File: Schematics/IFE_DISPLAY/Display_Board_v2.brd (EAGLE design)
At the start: 108 x 83.8 mm, 79 parts, among them U4 HEX_CONVERTER, U5 HEX_CONVERTER

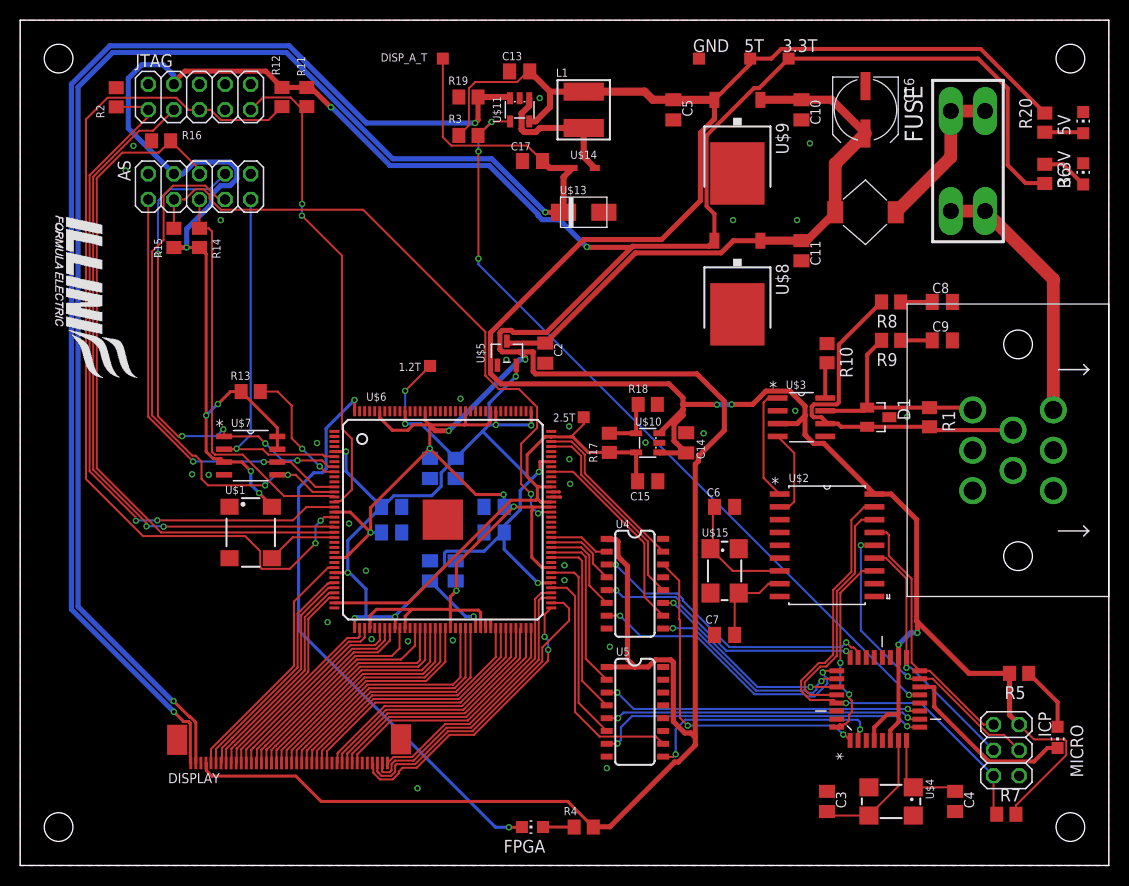
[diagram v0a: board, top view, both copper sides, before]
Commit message: Getting board size down on X axis so it is cheaper
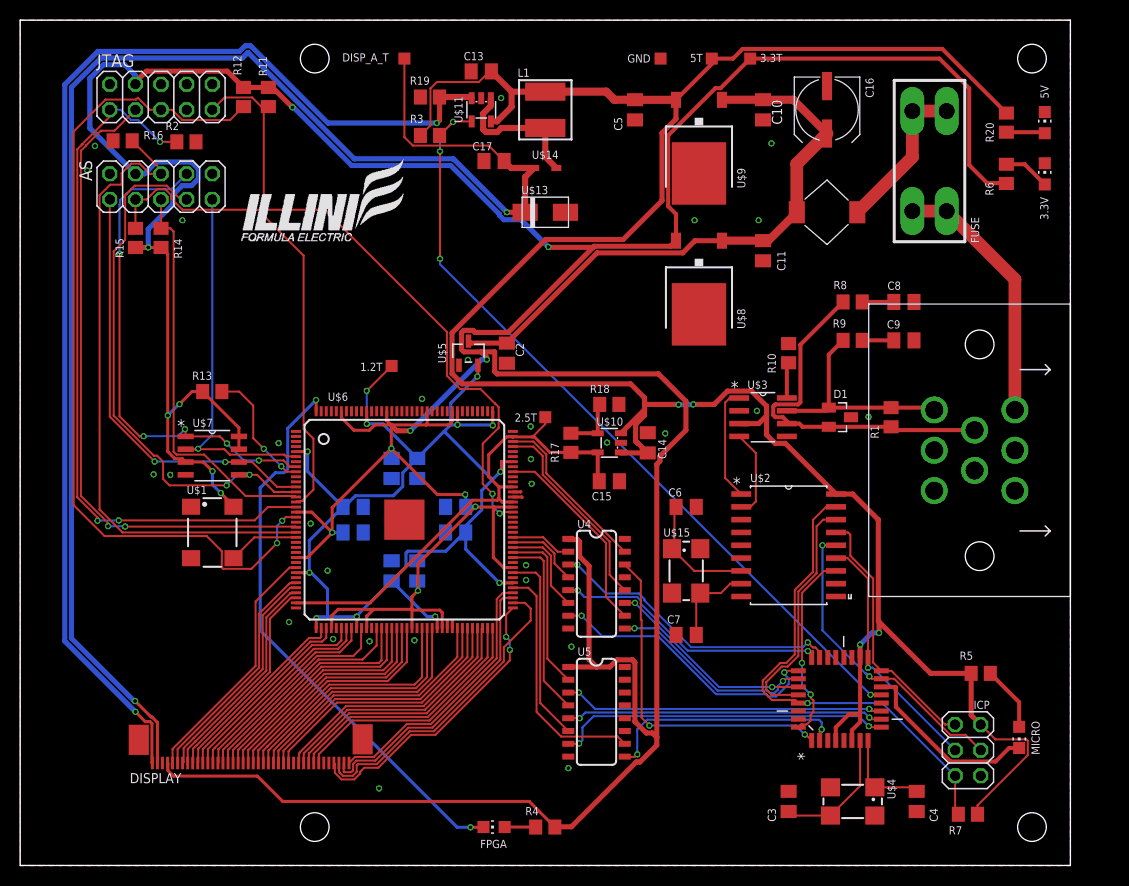
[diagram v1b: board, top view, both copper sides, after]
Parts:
- moved R2 8.24 mm to (16.5, 71.8), turned to 180 degrees
- moved C14 3.81 mm to (62.2, 41.9)
- moved 1.2T 3.81 mm to (36.8, 49.5)
- moved 2.5T 3.81 mm to (52.1, 44.5)
- moved 3.3T 3.81 mm to (72.4, 80.0)
- moved 3.3V 3.81 mm to (101.6, 68.6)
- moved 5T 3.81 mm to (68.6, 80.0)
- moved 5V 3.81 mm to (101.6, 73.7)
- moved ATMEGA328P 3.81 mm to (81.3, 16.5)
- moved C1 3.81 mm to (39.4, 39.4)
- moved C10 3.81 mm to (73.7, 74.9)
- moved C11 3.81 mm to (73.7, 61.0)
- moved C12 3.81 mm to (36.8, 39.4)
- moved C13 3.81 mm to (45.7, 78.7)
- moved C19 3.81 mm to (43.2, 35.6)
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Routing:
- net DISP_LEDA: track 154.8 -> 150.3 mm
- net DISP_LEDK: track 123.2 -> 118.7 mm
- net TMS: track 89.8 -> 85.5 mm
- net NCE: track 68.3 -> 64.5 mm
- net TCK: track 68.6 -> 71.2 mm, vias 2 -> 3
- net TDO: track 66.3 -> 64.1 mm
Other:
- board size 108 x 83.8 mm -> 104.1 x 83.8 mm

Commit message: Fixed board sizeing for cost efficiency + Aesthetic
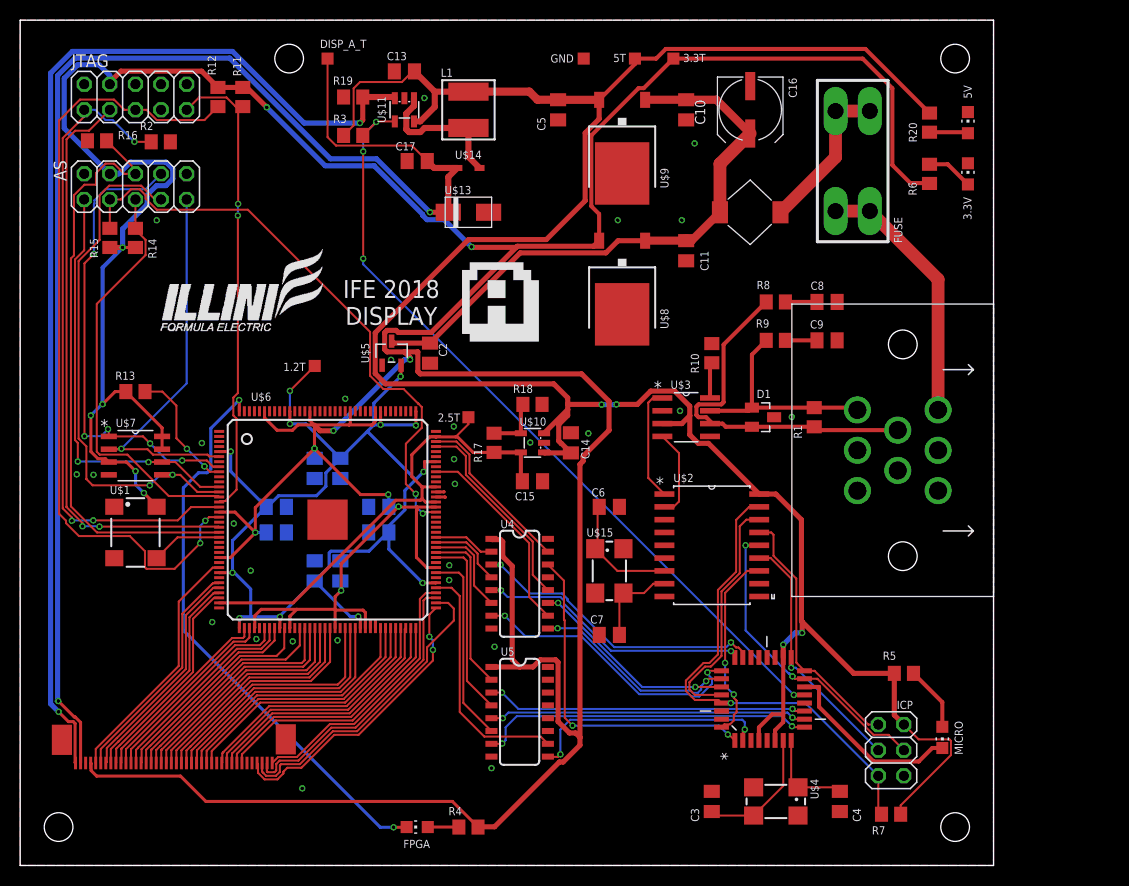
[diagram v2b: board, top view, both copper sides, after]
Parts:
- moved 3.3T 7.62 mm to (64.8, 80.0)
- moved ATMEGA328P 7.62 mm to (73.7, 16.5)
- moved C15 7.62 mm to (50.8, 38.1)
- moved C16 7.62 mm to (72.4, 74.9)
- moved C17 7.62 mm to (39.4, 69.8)
- moved C18 7.62 mm to (25.4, 33.0)
- moved C23 7.62 mm to (25.4, 35.6)
- moved C3 7.62 mm to (68.6, 6.35)
- moved C4 7.62 mm to (81.3, 6.35)
- moved C6 7.62 mm to (58.4, 35.6)
- moved C7 7.62 mm to (58.4, 22.9)
- moved D1 7.62 mm to (73.7, 44.5)
- moved FPGA 7.62 mm to (39.4, 3.81)
- moved FUSE 7.62 mm to (82.5, 69.8)
- moved ICP 7.62 mm to (86.4, 11.4)
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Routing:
- net DISP_LEDA: track 150.3 -> 141.7 mm
- net DISP_LEDK: track 118.7 -> 110.1 mm
- net TMS: track 85.5 -> 79.3 mm
- net TCK: track 71.2 -> 65.2 mm
- net TDO: track 64.1 -> 58.1 mm
- net +3V3: track 471.5 -> 465.9 mm
- net CONF_DONE: track 64.2 -> 59.2 mm
- net NCE: track 64.5 -> 59.7 mm
- net NCSO: track 49.7 -> 47.0 mm
- net ASDO: track 37.8 -> 39.9 mm
- net TDI: track 48.9 -> 47.2 mm
- net DATA0: track 53.5 -> 52.0 mm
- net NCONFIG: track 40.1 -> 41.4 mm
- net DCLK: track 42.9 -> 41.5 mm
- net GND: vias 30 -> 28
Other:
- board size 104.1 x 83.8 mm -> 96.5 x 83.8 mm
- board text added: "IFE 2018 DISPLAY"
